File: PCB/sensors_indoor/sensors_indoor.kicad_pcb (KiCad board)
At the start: 4 copper layers, 50 x 50 mm, 61 parts, among them J1 USB4125-GF-A, J2 STDC14, J3 B5B-ZR, Q1 DMN62D0U, SW1 SW_Push, U1 MIC5219-3.3YM5, U10 SPS30, U11 74LVC1G08, U2 STM32WBA5MMG, U3 FM24CL16B, U4 LPS22DF, U5 SHT45-AD1F, U6 SCD41-D-R2, U7 SGP41, U8 OPT4001DNPRQ1, U9 TSOP38436

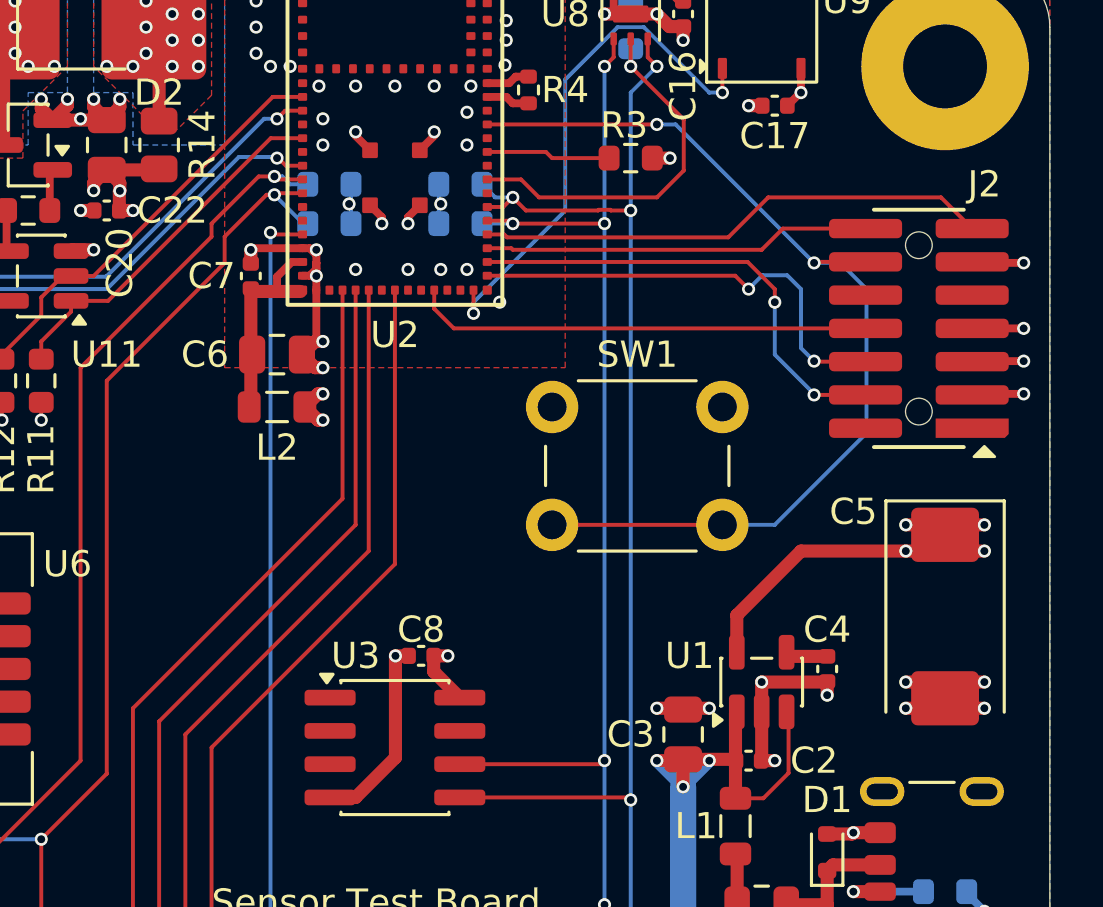
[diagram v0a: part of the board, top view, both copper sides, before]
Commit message: Changed switch to SMD type
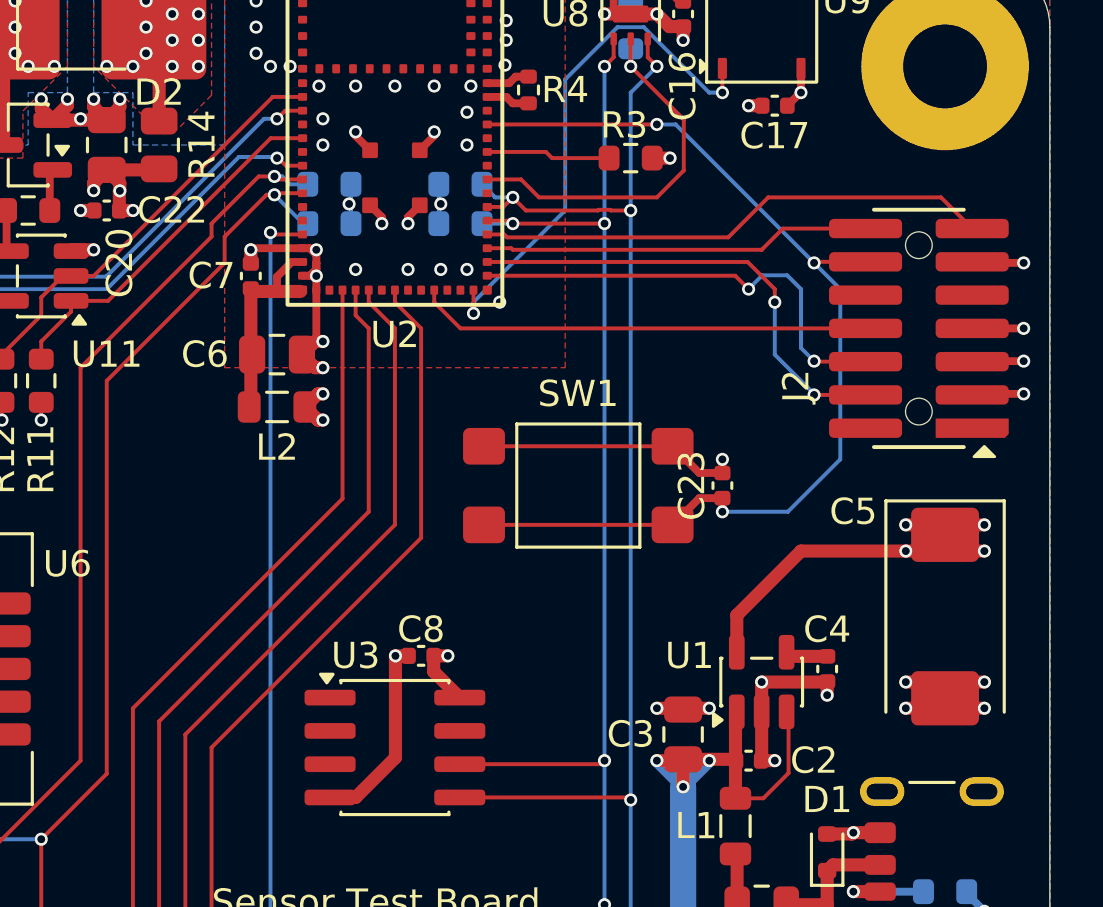
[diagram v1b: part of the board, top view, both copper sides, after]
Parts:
- added C23: 10n, Capacitor_SMD:C_0402_1005Metric, F.Cu at (112.5, 95.0)
- J2: footprint ZMPlib:SAMTEC_FTSH-107-01-L-DV-K-A -> DWlib:SAMTEC_FTSH-107-01-L-DV-K-A
- SW1: value SW_Push -> TL3305; footprint Button_Switch_THT:SW_PUSH_6mm -> DWlib:SW_Push_1P1T_NO_E-Switch_TL3305AFxxxQG
- moved SW1 3.16 mm to (107.0, 95.0)
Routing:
- net GND: track 95.7 -> 105.8 mm, vias 79 -> 80
- net /indoor_MCU/NRST: track 38.0 -> 39.9 mm, vias 2 -> 3
- net SPI_CS: track 41.1 -> 42.0 mm
- net SPI_MOSI: track 39.3 -> 40.1 mm

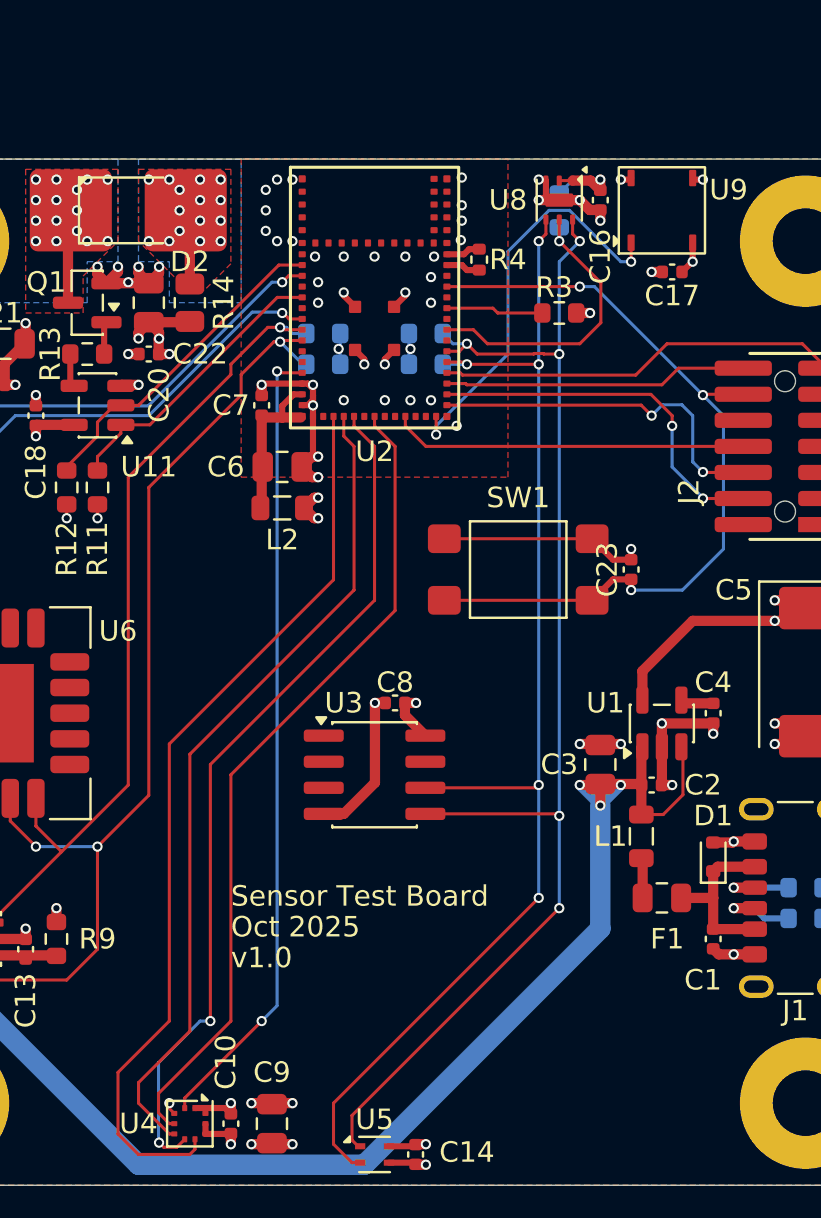
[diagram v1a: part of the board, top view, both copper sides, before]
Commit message: Added UV sensor
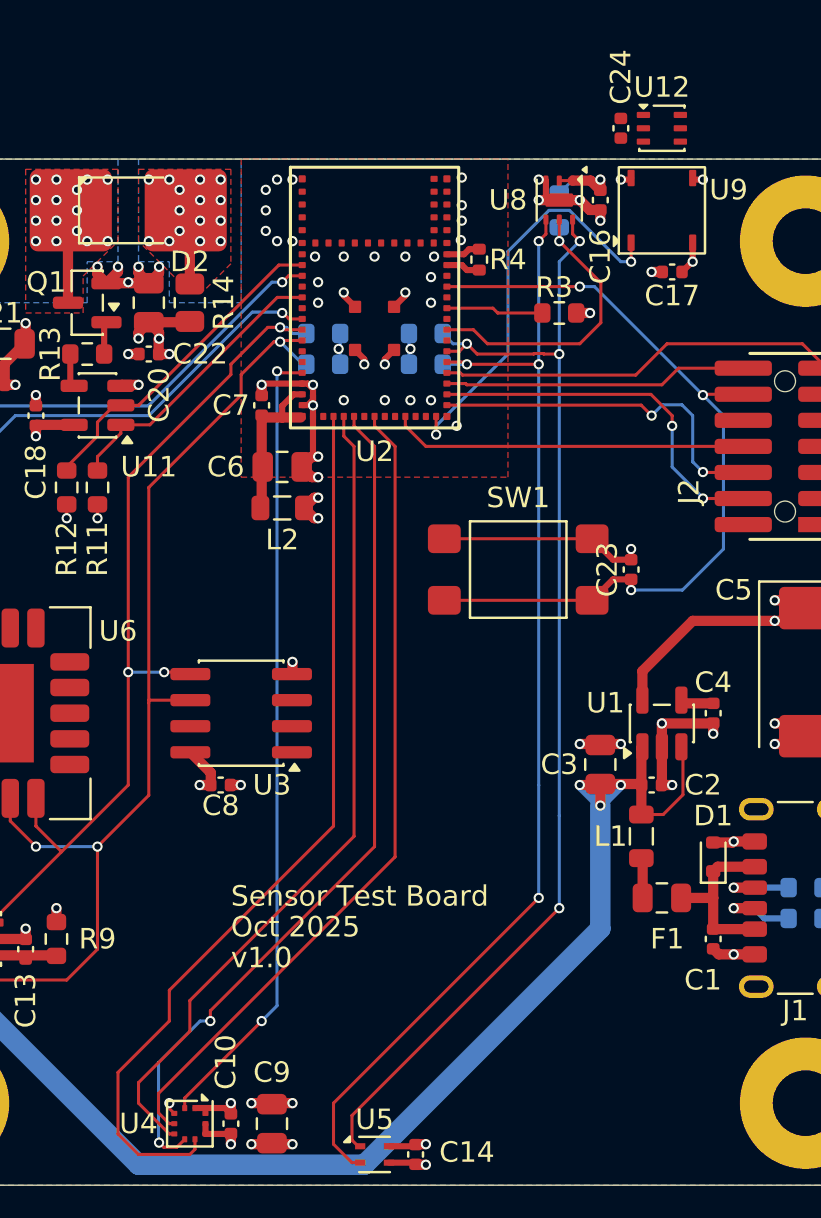
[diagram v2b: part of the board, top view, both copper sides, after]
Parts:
- added C24: 0.1u, Capacitor_SMD:C_0402_1005Metric, F.Cu at (112.0, 73.5)
- added U12: LTR-390UV-01, DWlib:Liteon_LTR-390UV-01, F.Cu at (114.0, 73.5)
- moved C8 9.39 mm to (92.5, 105.5), turned to 0 degrees
- moved U3 7.16 mm to (93.5, 102.0), turned to 180 degrees
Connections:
- U3 pad 5: I2C1_SDA -> I2C3_SDA
- U3 pad 6: I2C1_SCL -> I2C3_SCL
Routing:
- net I2C1_SDA: track 63.9 -> 57.4 mm, vias 5 -> 4
- net GND: track 105.8 -> 99.4 mm, vias 80 -> 81
- net I2C1_SCL: track 62.3 -> 56.7 mm, vias 5 -> 4
- net I2C3_SDA: track 40.7 -> 43.8 mm, vias 1 -> 3
- net I2C3_SCL: track 50.8 -> 52.8 mm

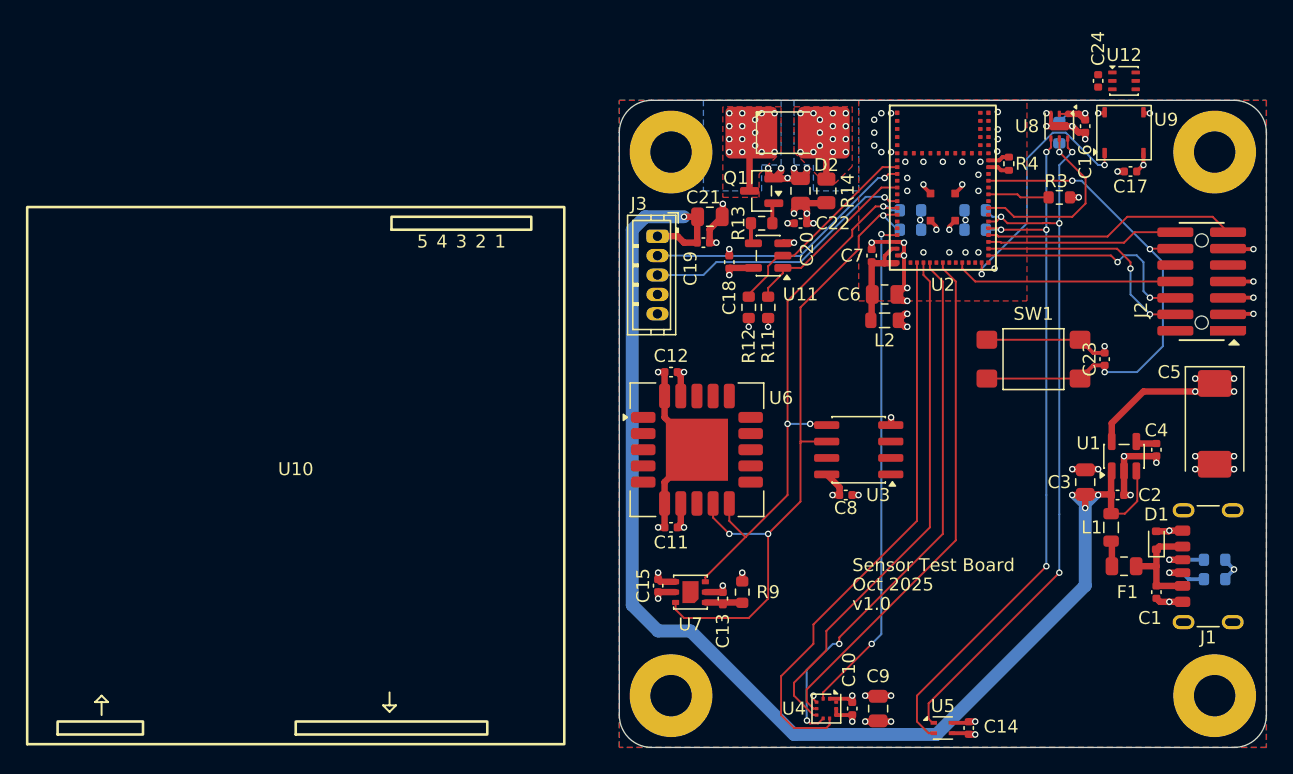
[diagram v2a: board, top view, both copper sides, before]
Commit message: Completed routing connections
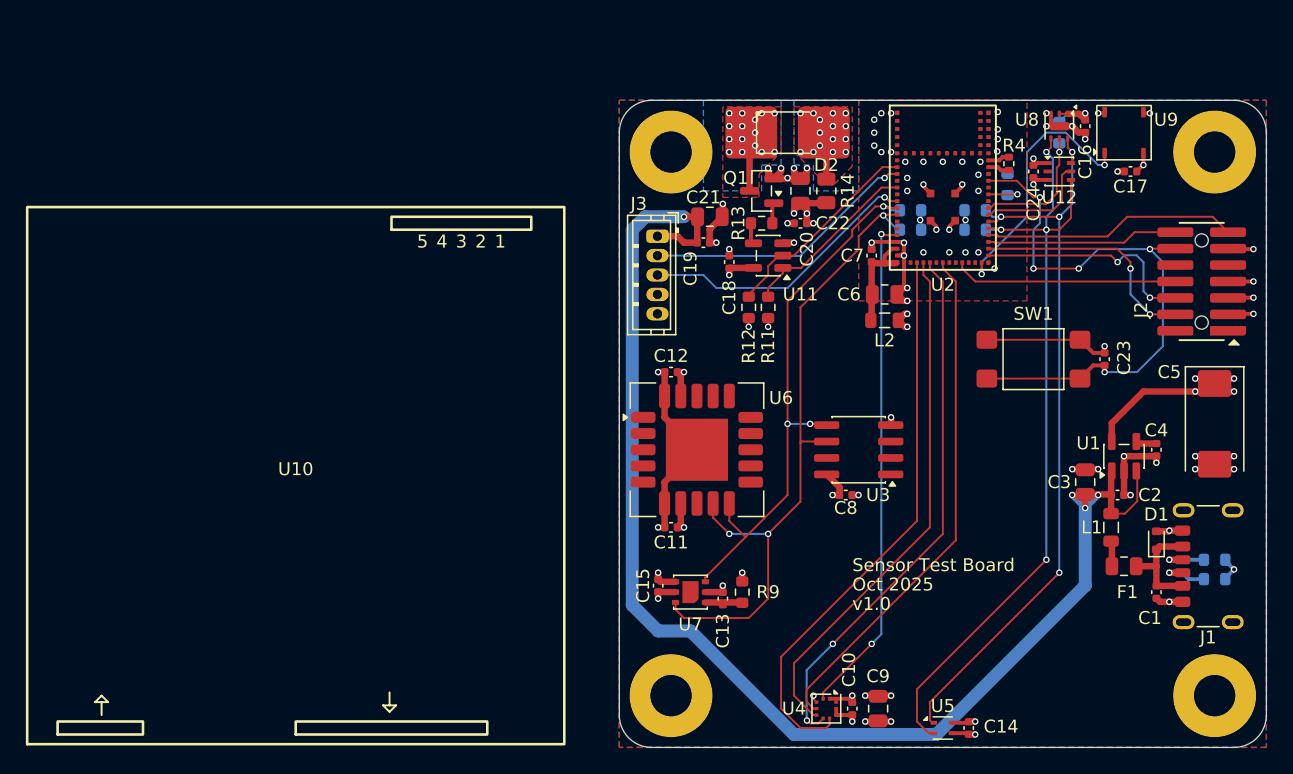
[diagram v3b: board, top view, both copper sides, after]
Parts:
- R3: moved to B.Cu
- moved C24 8.60 mm to (107.0, 80.5)
- moved U12 8.60 mm to (109.0, 80.5)
- moved R3 4.12 mm to (105.0, 81.5), turned to 90 degrees
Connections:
- U2 pad 43: unconnected-(U2-PB0-Pad43) -> INT_UV
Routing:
- net INT_UV: track 0.00 -> 8.93 mm
- net I2C1_SCL: track 56.7 -> 62.3 mm
- net /indoor_MCU/NRST: track 39.9 -> 45.1 mm, vias 3 -> 5
- net INT_ALS: track 14.7 -> 10.7 mm
- net /indoor_MCU/BOOT0: track 4.75 -> 3.03 mm, vias 0 -> 1
- net +3.3V: track 52.2 -> 53.9 mm, vias 24 -> 25
- net GND: track 99.4 -> 100.4 mm
- net UART_MISO: track 21.2 -> 22.0 mm
- net I2C1_SDA: track 57.4 -> 57.9 mm
